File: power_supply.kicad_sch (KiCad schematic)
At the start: 39 parts

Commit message: finished schematics
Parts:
- gave numbers to parts that had none: 36
- renumbered FB7 to FB21, FB8 to FB22, FB9 to FB23
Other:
- company: Thunderdrive GmbH -> UNIMOC universal motor controller
- title: UNIMOC Hardware 4850 -> (BCC) Battery Case Controller

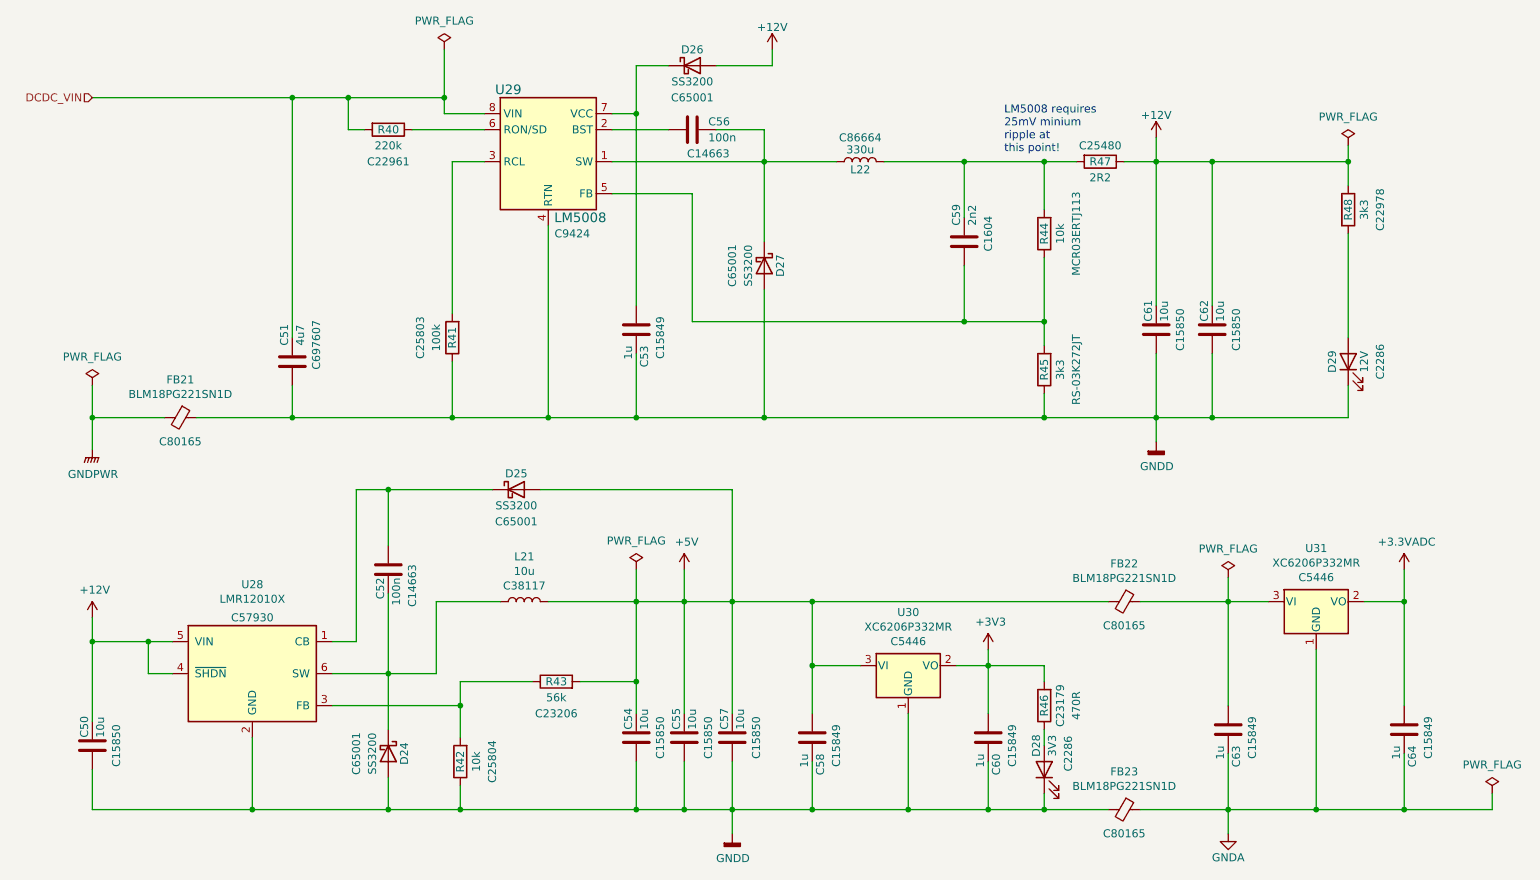
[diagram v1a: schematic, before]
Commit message: Placing first round finished
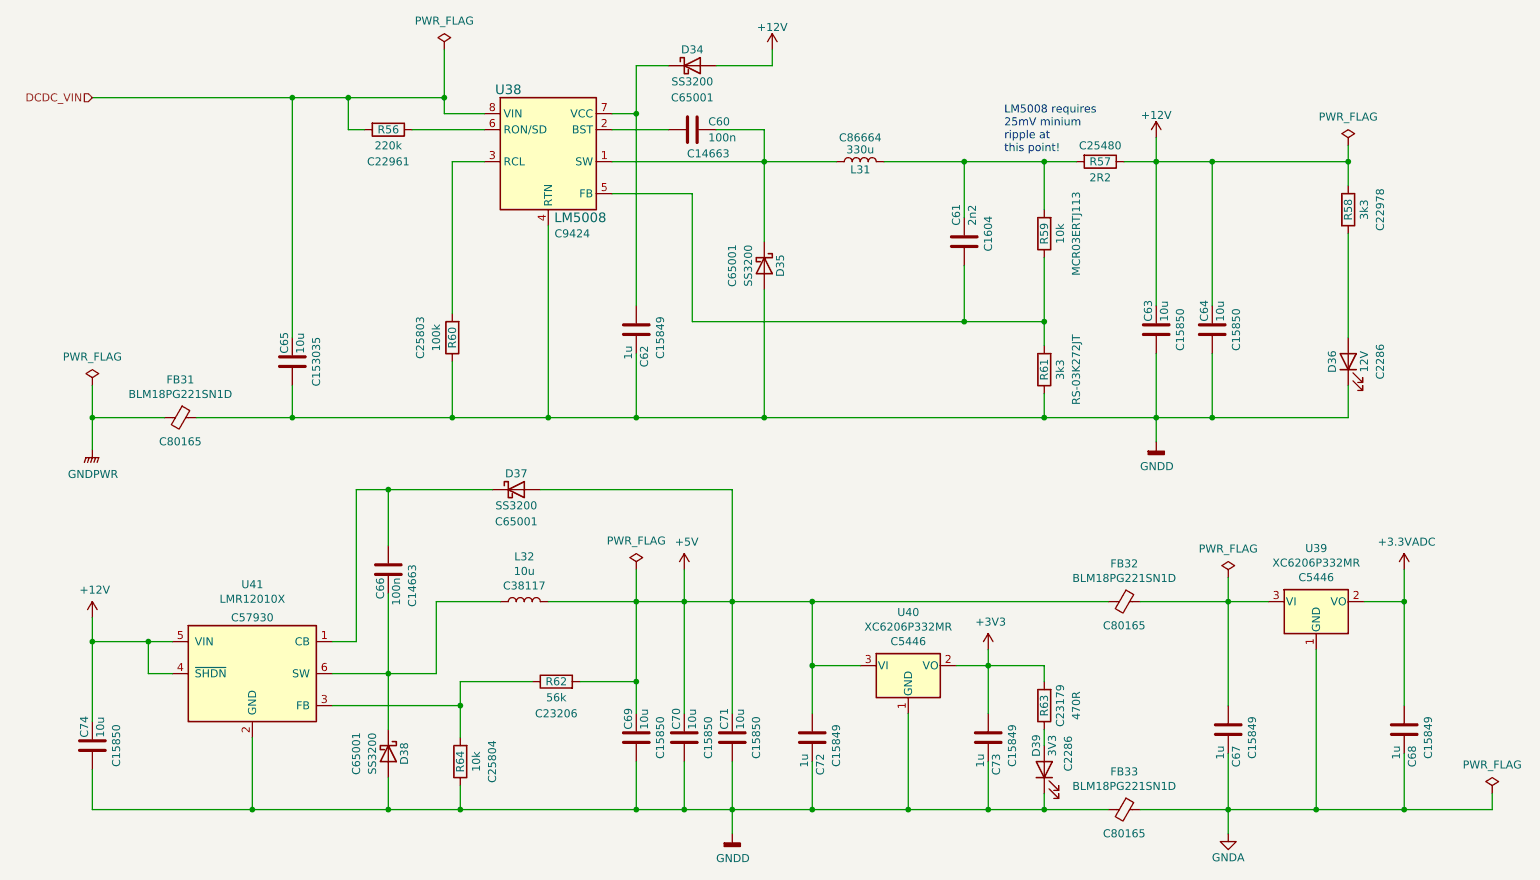
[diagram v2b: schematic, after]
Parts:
- removed C51: 4u7, Capacitor_SMD:C_1210_3225Metric, symbol Device:C
- added C65: 10u, Capacitor_SMD:C_2220_5650Metric, symbol Device:C
- renumbered C56 to C60, C59 to C61, C53 to C62, C61 to C63, C62 to C64, C52 to C66, C63 to C67, C64 to C68, C54 to C69, C55 to C70, C57 to C71, C58 to C72, C60 to C73, C50 to C74, D26 to D34, D27 to D35, D29 to D36, D25 to D37, D24 to D38, D28 to D39, FB21 to FB31, FB22 to FB32, FB23 to FB33, L22 to L31, L21 to L32, R40 to R56, R47 to R57, R48 to R58, R44 to R59, R41 to R60, R45 to R61, R43 to R62, R46 to R63, R42 to R64, U29 to U38, U31 to U39, U30 to U40, U28 to U41
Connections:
- net DCDC_VIN: now also C65.1
- net GNDD: now also C65.2

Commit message: just the silk open
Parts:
- renumbered C60 to C66, C61 to C67, C62 to C68, C63 to C69, C64 to C70, C65 to C71, C66 to C72, C67 to C73, C68 to C74, C69 to C75, C70 to C76, C71 to C77, C72 to C78, C73 to C79, C74 to C80, R56 to R59, R57 to R60, R58 to R61, R59 to R62, R60 to R63, R61 to R64, R62 to R65, R63 to R66, R64 to R67
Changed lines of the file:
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@@
   (symbol (lib_id "Device:R") (at 101.6 123.19 90) (unit 1)
     (in_bom yes) (on_board yes)
-    (property "Reference" "R62" (id 0) (at 101.6 123.19 90))
+    (property "Reference" "R65" (id 0) (at 101.6 123.19 90))
     (property "Value" "56k" (id 1) (at 101.6 125.73 90))
     (property "Footprint" "Resistor_SMD:R_0603_1608Metric" (id 2) (at 101.6 124.968 90)
@@
   (symbol (lib_id "Device:R") (at 85.09 68.58 180) (unit 1)
     (in_bom yes) (on_board yes)
-    (property "Reference" "R60" (id 0) (at 85.09 68.58 90))
+    (property "Reference" "R63" (id 0) (at 85.09 68.58 90))
     (property "Value" "100k" (id 1) (at 82.55 68.58 90))
     (property "Footprint" "Resistor_SMD:R_0603_1608Metric" (id 2) (at 86.868 68.58 90)
@@
   (symbol (lib_id "Device:C") (at 123.19 35.56 270) (unit 1)
     (in_bom yes) (on_board yes)
-    (property "Reference" "C60" (id 0) (at 125.73 34.29 90)
+    (property "Reference" "C66" (id 0) (at 125.73 34.29 90)
       (effects (font (size 1.27 1.27)) (justify left))
     )
@@
   (symbol (lib_id "Device:C") (at 142.24 132.08 180) (unit 1)
     (in_bom yes) (on_board yes)
-    (property "Reference" "C72" (id 0) (at 143.51 134.62 90)
+    (property "Reference" "C78" (id 0) (at 143.51 134.62 90)
       (effects (font (size 1.27 1.27)) (justify left))
     )
@@
   (symbol (lib_id "Device:C") (at 74.93 105.41 180) (unit 1)
     (in_bom yes) (on_board yes)
-    (property "Reference" "C66" (id 0) (at 73.66 106.68 90)
+    (property "Reference" "C72" (id 0) (at 73.66 106.68 90)
       (effects (font (size 1.27 1.27)) (justify left))
     )
@@
   (symbol (lib_id "Device:C") (at 114.3 132.08 0) (unit 1)
     (in_bom yes) (on_board yes)
-    (property "Reference" "C69" (id 0) (at 113.03 130.81 90)
+    (property "Reference" "C75" (id 0) (at 113.03 130.81 90)
       (effects (font (size 1.27 1.27)) (justify left))
     )
@@
   (symbol (lib_id "Device:R") (at 179.07 52.07 180) (unit 1)
     (in_bom yes) (on_board yes)
-    (property "Reference" "R59" (id 0) (at 179.07 52.07 90))
+    (property "Reference" "R62" (id 0) (at 179.07 52.07 90))
     (property "Value" "10k" (id 1) (at 181.61 52.07 90))
     (property "Footprint" "Resistor_SMD:R_0603_1608Metric" (id 2) (at 180.848 52.07 90)
@@
   (symbol (lib_id "Device:R") (at 187.96 40.64 270) (unit 1)
     (in_bom yes) (on_board yes)
-    (property "Reference" "R57" (id 0) (at 187.96 40.64 90))
+    (property "Reference" "R60" (id 0) (at 187.96 40.64 90))
     (property "Value" "2R2" (id 1) (at 187.96 43.18 90))
     (property "Footprint" "Resistor_SMD:R_2512_6332Metric" (id 2) (at 187.96 38.862 90)
@@
   (symbol (lib_id "Device:C") (at 129.54 132.08 0) (unit 1)
     (in_bom yes) (on_board yes)
-    (property "Reference" "C71" (id 0) (at 128.27 130.81 90)
+    (property "Reference" "C77" (id 0) (at 128.27 130.81 90)
       (effects (font (size 1.27 1.27)) (justify left))
     )
@@
   (symbol (lib_id "Device:C") (at 196.85 67.31 0) (unit 1)
     (in_bom yes) (on_board yes)
-    (property "Reference" "C63" (id 0) (at 195.58 66.04 90)
+    (property "Reference" "C69" (id 0) (at 195.58 66.04 90)
       (effects (font (size 1.27 1.27)) (justify left))
     )
@@
   (symbol (lib_id "Device:R") (at 179.07 73.66 180) (unit 1)
     (in_bom yes) (on_board yes)
-    (property "Reference" "R61" (id 0) (at 179.07 73.66 90))
+    (property "Reference" "R64" (id 0) (at 179.07 73.66 90))
     (property "Value" "3k3" (id 1) (at 181.61 73.66 90))
     (property "Footprint" "Resistor_SMD:R_0603_1608Metric" (id 2) (at 180.848 73.66 90)
@@
   (symbol (lib_id "Device:R") (at 179.07 127 180) (unit 1)
     (in_bom yes) (on_board yes)
-    (property "Reference" "R63" (id 0) (at 179.07 127 90))
+    (property "Reference" "R66" (id 0) (at 179.07 127 90))
     (property "Value" "470R" (id 1) (at 184.15 127 90))
     (property "Footprint" "Resistor_SMD:R_0603_1608Metric" (id 2) (at 180.848 127 90)
@@
   (symbol (lib_id "Device:C") (at 166.37 53.34 0) (unit 1)
     (in_bom yes) (on_board yes)
-    (property "Reference" "C61" (id 0) (at 165.1 50.8 90)
+    (property "Reference" "C67" (id 0) (at 165.1 50.8 90)
       (effects (font (size 1.27 1.27)) (justify left))
     )
@@
   (symbol (lib_id "Device:R") (at 74.93 35.56 270) (unit 1)
     (in_bom yes) (on_board yes)
-    (property "Reference" "R56" (id 0) (at 74.93 35.56 90))
+    (property "Reference" "R59" (id 0) (at 74.93 35.56 90))
     (property "Value" "220k" (id 1) (at 74.93 38.1 90))
     (property "Footprint" "Resistor_SMD:R_0603_1608Metric" (id 2) (at 74.93 33.782 90)
@@
   (symbol (lib_id "Device:C") (at 236.22 130.81 180) (unit 1)
     (in_bom yes) (on_board yes)
-    (property "Reference" "C68" (id 0) (at 237.49 133.35 90)
+    (property "Reference" "C74" (id 0) (at 237.49 133.35 90)
       (effects (font (size 1.27 1.27)) (justify left))
     )
@@
   (symbol (lib_id "Device:C") (at 121.92 132.08 0) (unit 1)
     (in_bom yes) (on_board yes)
-    (property "Reference" "C70" (id 0) (at 120.65 130.81 90)
+    (property "Reference" "C76" (id 0) (at 120.65 130.81 90)
       (effects (font (size 1.27 1.27)) (justify left))
     )
@@
   (symbol (lib_id "Device:C") (at 208.28 130.81 180) (unit 1)
     (in_bom yes) (on_board yes)
-    (property "Reference" "C67" (id 0) (at 209.55 133.35 90)
+    (property "Reference" "C73" (id 0) (at 209.55 133.35 90)
       (effects (font (size 1.27 1.27)) (justify left))
     )
@@
   (symbol (lib_id "Device:C") (at 170.18 132.08 180) (unit 1)
     (in_bom yes) (on_board yes)
-    (property "Reference" "C73" (id 0) (at 171.45 134.62 90)
+    (property "Reference" "C79" (id 0) (at 171.45 134.62 90)
       (effects (font (size 1.27 1.27)) (justify left))
     )
@@
   (symbol (lib_id "Device:C") (at 205.74 67.31 0) (unit 1)
     (in_bom yes) (on_board yes)
-    (property "Reference" "C64" (id 0) (at 204.47 66.04 90)
+    (property "Reference" "C70" (id 0) (at 204.47 66.04 90)
       (effects (font (size 1.27 1.27)) (justify left))
     )
@@
   (symbol (lib_id "Device:C") (at 59.69 72.39 0) (unit 1)
     (in_bom yes) (on_board yes)
-    (property "Reference" "C65" (id 0) (at 58.42 71.12 90)
+    (property "Reference" "C71" (id 0) (at 58.42 71.12 90)
       (effects (font (size 1.27 1.27)) (justify left))
     )
@@
   (symbol (lib_id "Device:R") (at 227.33 48.26 0) (unit 1)
     (in_bom yes) (on_board yes)
-    (property "Reference" "R58" (id 0) (at 227.33 48.26 90))
+    (property "Reference" "R61" (id 0) (at 227.33 48.26 90))
     (property "Value" "3k3" (id 1) (at 229.87 48.26 90))
     (property "Footprint" "Resistor_SMD:R_0603_1608Metric" (id 2) (at 225.552 48.26 90)
@@
   (symbol (lib_id "Device:R") (at 86.36 135.89 180) (unit 1)
     (in_bom yes) (on_board yes)
-    (property "Reference" "R64" (id 0) (at 86.36 135.89 90))
+    (property "Reference" "R67" (id 0) (at 86.36 135.89 90))
     (property "Value" "10k" (id 1) (at 88.9 135.89 90))
     (property "Footprint" "Resistor_SMD:R_0603_1608Metric" (id 2) (at 88.138 135.89 90)
@@
   (symbol (lib_id "Device:C") (at 27.94 133.35 0) (unit 1)
     (in_bom yes) (on_board yes)
-    (property "Reference" "C74" (id 0) (at 26.67 132.08 90)
+    (property "Reference" "C80" (id 0) (at 26.67 132.08 90)
       (effects (font (size 1.27 1.27)) (justify left))
     )
@@
   (symbol (lib_id "Device:C") (at 114.3 67.31 180) (unit 1)
     (in_bom yes) (on_board yes)
-    (property "Reference" "C62" (id 0) (at 115.57 69.85 90)
-      (effects (font (size 1.27 1.27)) (justify left))
-    )
+    (property "Reference" "C68" (id 0) (at 115.57 69.85 90)
+      (effects (font (size 1.27 1.27)) (justify left))
+    )
